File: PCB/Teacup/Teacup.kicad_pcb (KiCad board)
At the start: 2 copper layers, 1 part

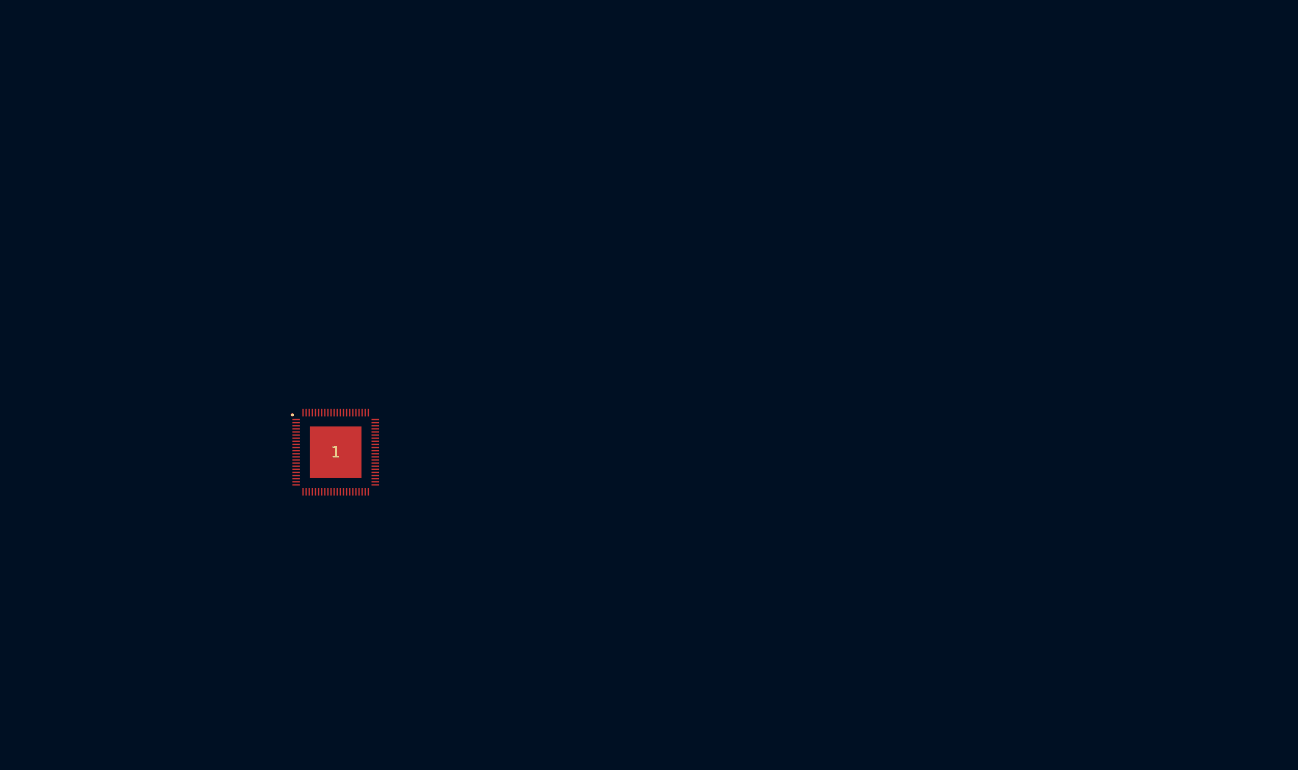
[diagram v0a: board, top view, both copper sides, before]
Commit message: pcb: flash + footprints
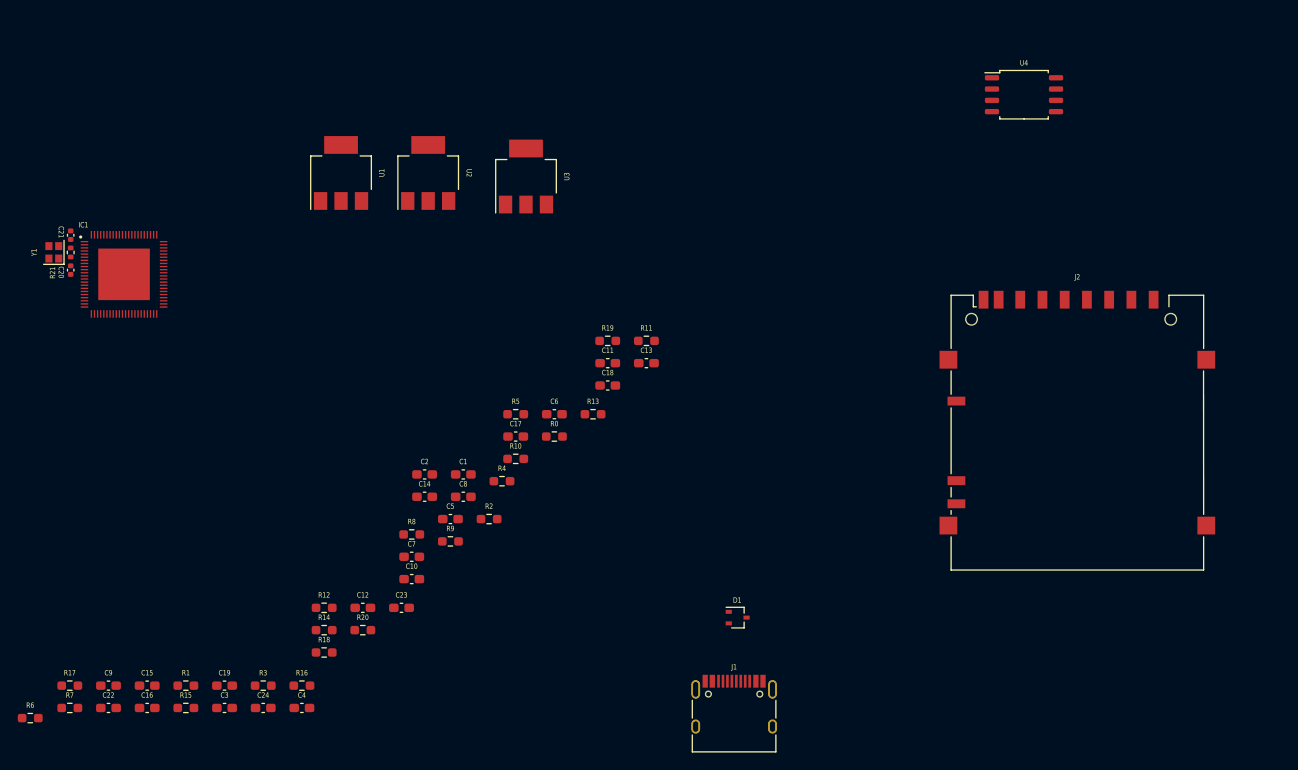
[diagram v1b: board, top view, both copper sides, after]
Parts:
- removed 1: T31ZX, Footprints:QFN35P900X900X90-89N-D
- added C1: 10uF, Capacitor_SMD:C_0603_1608Metric_Pad1.08x0.95mm_HandSolder, F.Cu at (160.2, 101.7)
- added C10: 10uF, Capacitor_SMD:C_0603_1608Metric_Pad1.08x0.95mm_HandSolder, F.Cu at (154.3, 113.5)
- added C11: 1uF, Capacitor_SMD:C_0603_1608Metric_Pad1.08x0.95mm_HandSolder, F.Cu at (176.4, 89.2)
- added C12: 100nF, Capacitor_SMD:C_0603_1608Metric_Pad1.08x0.95mm_HandSolder, F.Cu at (148.8, 116.7)
- added C13: 10uF, Capacitor_SMD:C_0603_1608Metric_Pad1.08x0.95mm_HandSolder, F.Cu at (180.7, 89.2)
- added C14: 1uF, Capacitor_SMD:C_0603_1608Metric_Pad1.08x0.95mm_HandSolder, F.Cu at (155.8, 104.2)
- added C15: 100nF, Capacitor_SMD:C_0603_1608Metric_Pad1.08x0.95mm_HandSolder, F.Cu at (124.6, 125.5)
- added C16: 10uF, Capacitor_SMD:C_0603_1608Metric_Pad1.08x0.95mm_HandSolder, F.Cu at (124.6, 128.0)
- added C17: 1uF, Capacitor_SMD:C_0603_1608Metric_Pad1.08x0.95mm_HandSolder, F.Cu at (166.0, 97.4)
- added C18: 100nF, Capacitor_SMD:C_0603_1608Metric_Pad1.08x0.95mm_HandSolder, F.Cu at (176.4, 91.7)
- added C19: 100nF, Capacitor_SMD:C_0603_1608Metric_Pad1.08x0.95mm_HandSolder, F.Cu at (133.3, 125.5)
- added C2: 1uF, Capacitor_SMD:C_0603_1608Metric_Pad1.08x0.95mm_HandSolder, F.Cu at (155.8, 101.7)
- added C20: TBD, Capacitor_SMD:C_0402_1005Metric, F.Cu at (116.0, 78.7)
- added C21: TBD, Capacitor_SMD:C_0402_1005Metric, F.Cu at (116.0, 74.8)
- added C22: 4.7uF, Capacitor_SMD:C_0603_1608Metric_Pad1.08x0.95mm_HandSolder, F.Cu at (120.2, 128.0)
- added C23: 100nF, Capacitor_SMD:C_0603_1608Metric_Pad1.08x0.95mm_HandSolder, F.Cu at (153.2, 116.7)
- added C24: 100nF, Capacitor_SMD:C_0603_1608Metric_Pad1.08x0.95mm_HandSolder, F.Cu at (137.7, 128.0)
- added C3: 100nF, Capacitor_SMD:C_0603_1608Metric_Pad1.08x0.95mm_HandSolder, F.Cu at (133.3, 128.0)
- added C4: 10uF, Capacitor_SMD:C_0603_1608Metric_Pad1.08x0.95mm_HandSolder, F.Cu at (142.0, 128.0)
- added C5: 1uF, Capacitor_SMD:C_0603_1608Metric_Pad1.08x0.95mm_HandSolder, F.Cu at (158.7, 106.7)
- added C6: 100nF, Capacitor_SMD:C_0603_1608Metric_Pad1.08x0.95mm_HandSolder, F.Cu at (170.4, 94.9)
- added C7: 10uF, Capacitor_SMD:C_0603_1608Metric_Pad1.08x0.95mm_HandSolder, F.Cu at (154.3, 111.0)
- added C8: 1uF, Capacitor_SMD:C_0603_1608Metric_Pad1.08x0.95mm_HandSolder, F.Cu at (160.2, 104.2)
- added C9: 100nF, Capacitor_SMD:C_0603_1608Metric_Pad1.08x0.95mm_HandSolder, F.Cu at (120.2, 125.5)
- added D1: D_TVS_Dual_AAC, Package_TO_SOT_SMD:SOT-323_SC-70, F.Cu at (191.0, 117.8)
- added IC1: T31ZX, Footprints:QFN35P900X900X90-89N-D, F.Cu at (122.0, 79.2)
- added J1: USB_C_Receptacle_USB2.0, Connector_USB:USB_C_Receptacle_HRO_TYPE-C-31-M-12, F.Cu at (190.6, 129.0)
- added J2: SD_Card, Connector_Card:SD_Hirose_DM1AA_SF_PEJ82, F.Cu at (229.2, 97.0)
- added R0: 100k, Resistor_SMD:R_0603_1608Metric_Pad0.98x0.95mm_HandSolder, F.Cu at (170.4, 97.4)
- added R1: 100k, Resistor_SMD:R_0603_1608Metric_Pad0.98x0.95mm_HandSolder, F.Cu at (128.9, 125.5)
- added R10: 100k, Resistor_SMD:R_0603_1608Metric_Pad0.98x0.95mm_HandSolder, F.Cu at (166.0, 100.0)
- added R11: 100k, Resistor_SMD:R_0603_1608Metric_Pad0.98x0.95mm_HandSolder, F.Cu at (180.7, 86.7)
- added R12: 100k, Resistor_SMD:R_0603_1608Metric_Pad0.98x0.95mm_HandSolder, F.Cu at (144.5, 116.7)
- added R13: 100k, Resistor_SMD:R_0603_1608Metric_Pad0.98x0.95mm_HandSolder, F.Cu at (174.7, 94.9)
- added R14: 100k, Resistor_SMD:R_0603_1608Metric_Pad0.98x0.95mm_HandSolder, F.Cu at (144.5, 119.2)
- added R15: 47k, Resistor_SMD:R_0603_1608Metric_Pad0.98x0.95mm_HandSolder, F.Cu at (128.9, 128.0)
- added R16: 47k, Resistor_SMD:R_0603_1608Metric_Pad0.98x0.95mm_HandSolder, F.Cu at (142.0, 125.5)
- added R17: 47k, Resistor_SMD:R_0603_1608Metric_Pad0.98x0.95mm_HandSolder, F.Cu at (115.9, 125.5)
- added R18: 47k, Resistor_SMD:R_0603_1608Metric_Pad0.98x0.95mm_HandSolder, F.Cu at (144.5, 121.7)
- added R19: 47k, Resistor_SMD:R_0603_1608Metric_Pad0.98x0.95mm_HandSolder, F.Cu at (176.4, 86.7)
- added R2: 0R, Resistor_SMD:R_0603_1608Metric_Pad0.98x0.95mm_HandSolder, F.Cu at (163.1, 106.7)
- added R20: 47k, Resistor_SMD:R_0603_1608Metric_Pad0.98x0.95mm_HandSolder, F.Cu at (148.8, 119.2)
- added R21: 1M, Resistor_SMD:R_0402_1005Metric, F.Cu at (116.0, 76.7)
- added R3: 0R, Resistor_SMD:R_0603_1608Metric_Pad0.98x0.95mm_HandSolder, F.Cu at (137.7, 125.5)
- added R4: 5k1, Resistor_SMD:R_0603_1608Metric_Pad0.98x0.95mm_HandSolder, F.Cu at (164.5, 102.5)
- added R5: 5k1, Resistor_SMD:R_0603_1608Metric_Pad0.98x0.95mm_HandSolder, F.Cu at (166.0, 94.9)
- added R6: 0R, Resistor_SMD:R_0603_1608Metric_Pad0.98x0.95mm_HandSolder, F.Cu at (111.5, 129.1)
- added R7: 0R, Resistor_SMD:R_0603_1608Metric_Pad0.98x0.95mm_HandSolder, F.Cu at (115.9, 128.0)
- added R8: 0R, Resistor_SMD:R_0603_1608Metric_Pad0.98x0.95mm_HandSolder, F.Cu at (154.3, 108.5)
- added R9: 0R, Resistor_SMD:R_0603_1608Metric_Pad0.98x0.95mm_HandSolder, F.Cu at (158.7, 109.2)
- added U1: AZ1117-3.3, Kicad:SOT-223-3_TabPin2, F.Cu at (146.4, 67.8)
- added U2: AZ1117-1.8, Kicad:SOT-223-3_TabPin2, F.Cu at (156.2, 67.8)
- added U3: MCP1826S, Kicad:SOT-223-3_TabPin2, F.Cu at (167.2, 68.2)
- added U4: W25Q32JVSS, Package_SO:SOIC-8_5.23x5.23mm_P1.27mm, F.Cu at (223.2, 59.0)
- added Y1: 24 MHz, Crystal:Crystal_SMD_2016-4Pin_2.0x1.6mm, F.Cu at (114.1, 76.7)

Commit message: pcb: sch done, initial placement
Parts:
- added J3: SFW15R-2STE1LF, Footprints:SFW15R2STE1LF, F.Cu at (174.4, 96.3)
- added J4: EXP0, Connector_PinHeader_2.54mm:PinHeader_1x10_P2.54mm_Vertical, F.Cu at (165.4, 85.2)
- added J5: UART, Connector_PinHeader_2.54mm:PinHeader_1x03_P2.54mm_Vertical, F.Cu at (208.9, 54.8)
- added J6: EXP2, Connector_PinHeader_2.54mm:PinHeader_1x16_P2.54mm_Vertical, F.Cu at (165.3, 54.8)
- added J7: EXP1, Connector_PinHeader_2.54mm:PinHeader_1x16_P2.54mm_Vertical, F.Cu at (203.4, 58.4)
- moved R6 136.0 mm to (233.0, 68.0), turned to 90 degrees
- moved C16 134.5 mm to (243.4, 64.8), turned to 180 degrees
- moved C15 131.9 mm to (239.8, 61.2)
- moved R7 128.5 mm to (229.6, 68.0), turned to 90 degrees
- moved C9 128.1 mm to (233.1, 64.8)
- moved C3 111.7 mm to (222.8, 61.2)
- moved R17 110.6 mm to (217.2, 81.0), turned to 90 degrees
- moved R15 103.5 mm to (217.2, 73.8), turned to 90 degrees
- moved R3 99.8 mm to (219.2, 68.0), turned to 90 degrees
- moved C4 99.7 mm to (219.2, 64.8), turned to 180 degrees
- moved C12 98.0 mm to (229.6, 61.2), turned to 180 degrees
- moved R8 94.5 mm to (239.8, 68.0), turned to 90 degrees
- moved R9 94.2 mm to (243.4, 68.0), turned to 90 degrees
- moved C14 93.6 mm to (239.8, 63.0)
- moved C7 93.2 mm to (233.2, 61.2)
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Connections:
- IC1 pad 1: unconnected-(IC1-Pad1) -> Net-(IC1-Pad1)
- IC1 pad 11: unconnected-(IC1-Pad11) -> /CAM_PE
- IC1 pad 12: unconnected-(IC1-Pad12) -> /I2C0_SCK
- IC1 pad 13: unconnected-(IC1-Pad13) -> /I2C0_SDA
- IC1 pad 14: unconnected-(IC1-Pad14) -> /PA17
- IC1 pad 15: unconnected-(IC1-Pad15) -> /PA16
- IC1 pad 16: unconnected-(IC1-Pad16) -> /PA15
- IC1 pad 17: unconnected-(IC1-Pad17) -> /PA14
- IC1 pad 18: unconnected-(IC1-Pad18) -> /PA11
- IC1 pad 19: unconnected-(IC1-Pad19) -> /PA10
- IC1 pad 2: unconnected-(IC1-Pad2) -> Net-(IC1-Pad2)
- IC1 pad 20: unconnected-(IC1-Pad20) -> /PA09
- IC1 pad 21: unconnected-(IC1-Pad21) -> /PA08
- IC1 pad 22: unconnected-(IC1-Pad22) -> /PA07
- IC1 pad 23: unconnected-(IC1-Pad23) -> /PA06
- IC1 pad 24: unconnected-(IC1-Pad24) -> /MIPI_0_N
- IC1 pad 25: unconnected-(IC1-Pad25) -> /MIPI_0_P
- IC1 pad 26: unconnected-(IC1-Pad26) -> /MIPI_CLK_N
- IC1 pad 27: unconnected-(IC1-Pad27) -> /MIPI_CLK_P
- IC1 pad 28: unconnected-(IC1-Pad28) -> /MIPI_1_N
- IC1 pad 29: unconnected-(IC1-Pad29) -> /MIPI_1_P
- IC1 pad 32: unconnected-(IC1-Pad32) -> /AUX0
- IC1 pad 41: unconnected-(IC1-Pad41) -> /MICLP
- IC1 pad 44: unconnected-(IC1-Pad44) -> /HPOUTL
- IC1 pad 57: unconnected-(IC1-Pad57) -> Net-(IC1-Pad57)
- IC1 pad 58: unconnected-(IC1-Pad58) -> Net-(IC1-Pad58)
- IC1 pad 59: unconnected-(IC1-Pad59) -> Net-(IC1-Pad59)
- IC1 pad 60: unconnected-(IC1-Pad60) -> Net-(IC1-Pad60)
- IC1 pad 61: unconnected-(IC1-Pad61) -> Net-(IC1-Pad61)
- IC1 pad 62: unconnected-(IC1-Pad62) -> Net-(IC1-Pad62)
- IC1 pad 63: unconnected-(IC1-Pad63) -> Net-(IC1-Pad63)
- IC1 pad 64: unconnected-(IC1-Pad64) -> Net-(IC1-Pad64)
- IC1 pad 65: unconnected-(IC1-Pad65) -> Net-(IC1-Pad65)
- IC1 pad 66: unconnected-(IC1-Pad66) -> Net-(IC1-Pad66)
- IC1 pad 68: unconnected-(IC1-Pad68) -> Net-(IC1-Pad68)
- IC1 pad 69: unconnected-(IC1-Pad69) -> Net-(IC1-Pad69)
- IC1 pad 70: unconnected-(IC1-Pad70) -> Net-(IC1-Pad70)
- IC1 pad 71: unconnected-(IC1-Pad71) -> Net-(IC1-Pad71)
- IC1 pad 73: unconnected-(IC1-Pad73) -> /UART_RX
- IC1 pad 74: unconnected-(IC1-Pad74) -> /UART_TX
- IC1 pad 80: unconnected-(IC1-Pad80) -> /CAM_LED
- IC1 pad 81: unconnected-(IC1-Pad81) -> /PB30
- IC1 pad 82: unconnected-(IC1-Pad82) -> /PB29
- IC1 pad 85: unconnected-(IC1-Pad85) -> /PB28
- IC1 pad 86: unconnected-(IC1-Pad86) -> /PB27
- IC1 pad 87: unconnected-(IC1-Pad87) -> /PB26
- IC1 pad 88: unconnected-(IC1-Pad88) -> /PB25
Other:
- board outline added: 89.6 x 50.4 mm

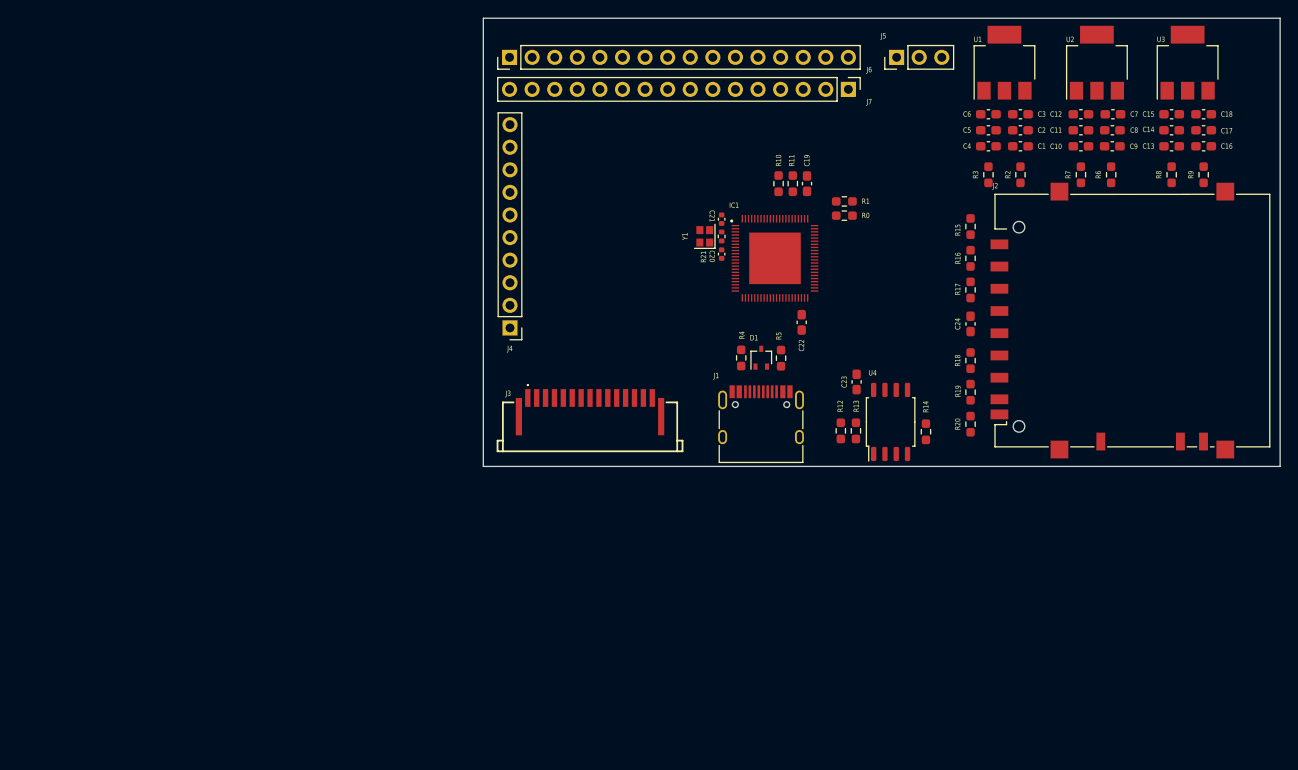
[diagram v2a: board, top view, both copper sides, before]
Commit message: pcb: routed high speed signals
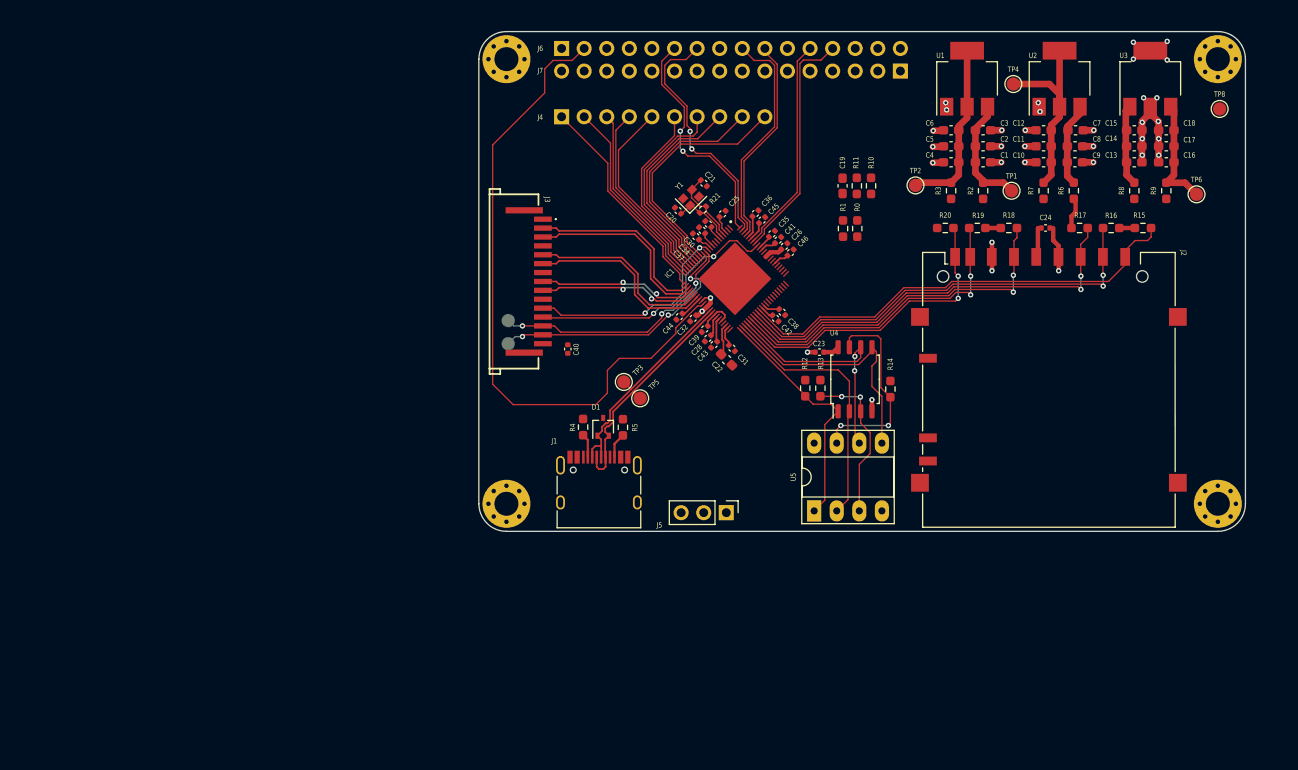
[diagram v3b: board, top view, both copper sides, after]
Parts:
- added C25: 100nF, Capacitor_SMD:C_0402_1005Metric, F.Cu at (189.3, 72.4)
- added C26: 100nF, Capacitor_SMD:C_0402_1005Metric, F.Cu at (196.2, 76.0)
- added C28: 100nF, Capacitor_SMD:C_0402_1005Metric, F.Cu at (187.7, 86.4)
- added C30: 100nF, Capacitor_SMD:C_0402_1005Metric, F.Cu at (187.7, 73.5)
- added C31: 100nF, Capacitor_SMD:C_0402_1005Metric, F.Cu at (190.3, 87.5)
- added C32: 100nF, Capacitor_SMD:C_0402_1005Metric, F.Cu at (186.0, 84.2)
- added C34: 100nF, Capacitor_SMD:C_0402_1005Metric, F.Cu at (187.0, 74.2)
- added C35: 100nF, Capacitor_SMD:C_0402_1005Metric, F.Cu at (194.8, 74.7)
- added C36: 100nF, Capacitor_SMD:C_0402_1005Metric, F.Cu at (193.0, 72.3)
- added C37: 100nF, Capacitor_SMD:C_0402_1005Metric, F.Cu at (186.3, 75.0)
- added C38: 100nF, Capacitor_SMD:C_0402_1005Metric, F.Cu at (196.0, 83.5)
- added C39: 100nF, Capacitor_SMD:C_0402_1005Metric, F.Cu at (187.3, 85.3)
- added C40: 100nF, Capacitor_SMD:C_0402_1005Metric, F.Cu at (171.9, 87.6)
- added C41: 100nF, Capacitor_SMD:C_0402_1005Metric, F.Cu at (195.6, 75.3)
- added C42: 100nF, Capacitor_SMD:C_0402_1005Metric, F.Cu at (195.2, 84.2)
- added C43: 100nF, Capacitor_SMD:C_0402_1005Metric, F.Cu at (188.3, 87.1)
- added C44: 100nF, Capacitor_SMD:C_0402_1005Metric, F.Cu at (184.4, 84.0)
- added C45: 100nF, Capacitor_SMD:C_0402_1005Metric, F.Cu at (193.8, 73.1)
- added C46: 100nF, Capacitor_SMD:C_0402_1005Metric, F.Cu at (196.9, 76.8)
- added REF**: MountingHole_2.7mm_M2.5_Pad_Via, MountingHole:MountingHole_2.7mm_M2.5_Pad_Via, F.Cu at (245.0, 55.0)
- added REF**: MountingHole_2.7mm_M2.5_Pad_Via, MountingHole:MountingHole_2.7mm_M2.5_Pad_Via, F.Cu at (245.0, 105.0)
- added REF**: MountingHole_2.7mm_M2.5_Pad_Via, MountingHole:MountingHole_2.7mm_M2.5_Pad_Via, F.Cu at (165.0, 105.0)
- added REF**: MountingHole_2.7mm_M2.5_Pad_Via, MountingHole:MountingHole_2.7mm_M2.5_Pad_Via, F.Cu at (165.0, 55.0)
- added TP1: TestPoint, TestPoint:TestPoint_Pad_D1.5mm, F.Cu at (221.8, 69.8)
- added TP2: TestPoint, TestPoint:TestPoint_Pad_D1.5mm, F.Cu at (211.0, 69.2)
- added TP3: TestPoint, TestPoint:TestPoint_Pad_D1.5mm, F.Cu at (178.2, 91.3)
- added TP4: TestPoint, TestPoint:TestPoint_Pad_D1.5mm, F.Cu at (222.0, 57.8)
- added TP5: TestPoint, TestPoint:TestPoint_Pad_D1.5mm, F.Cu at (180.0, 93.1)
- added TP6: TestPoint, TestPoint:TestPoint_Pad_D1.5mm, F.Cu at (242.6, 70.2)
- added TP7: TestPoint, TestPoint:TestPoint_Pad_D1.5mm, B.Cu at (165.2, 87.0)
- added TP8: TestPoint, TestPoint:TestPoint_Pad_D1.5mm, F.Cu at (245.2, 60.6)
- added TP9: TestPoint, TestPoint:TestPoint_Pad_D1.5mm, B.Cu at (165.2, 84.4)
- added U5: W25Q32JVSS, Package_DIP:DIP-8_W7.62mm_Socket_LongPads, F.Cu at (199.6, 105.8)
- C23, C24: footprint Capacitor_SMD:C_0603_1608Metric_Pad1.08x0.95mm_HandSolder -> Capacitor_SMD:C_0402_1005Metric
- J1: value USB_C_Receptacle_USB2.0 -> USB Type-C
- moved J5 54.7 mm to (189.7, 106.0), turned to -90 degrees
- moved J4 24.4 mm to (171.2, 61.5), turned to 90 degrees
- moved R20 22.2 mm to (214.3, 74.0), turned to 0 degrees
- moved J1 19.7 mm to (175.4, 103.8)
- moved R4 19.4 mm to (173.6, 96.4)
- moved R5 19.4 mm to (178.1, 96.4)
- moved D1 19.4 mm to (175.9, 96.3)
- moved R15 19.4 mm to (236.6, 74.0), turned to 0 degrees
- moved R19 18.5 mm to (217.9, 74.0), turned to 180 degrees
- moved J3 18.5 mm to (165.8, 80.0), turned to -90 degrees
- moved R16 16.2 mm to (233.0, 74.0), turned to 180 degrees
- moved R18 15.5 mm to (221.5, 74.0), turned to 0 degrees
- moved R17 14.1 mm to (229.4, 74.0), turned to 0 degrees
- moved C24 13.7 mm to (225.6, 74.0), turned to 0 degrees
- moved J2 12.2 mm to (226.0, 92.2), turned to 0 degrees
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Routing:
- net /AUX0: track 0.00 -> 74.5 mm
- net /MMC0_D2: track 0.00 -> 51.6 mm
- net /MMC0_D3: track 0.00 -> 49.1 mm, vias 0 -> 2
- net /MMC0_CMD: track 0.00 -> 47.6 mm, vias 0 -> 2
- net /MMC0_CLK: track 0.00 -> 40.4 mm, vias 0 -> 2
- net GND: track 0.00 -> 37.5 mm, vias 0 -> 33
- net /MMC0_D0: track 0.00 -> 36.0 mm, vias 0 -> 2
- net /MMC0_D1: track 0.00 -> 35.2 mm, vias 0 -> 2
- net /I2C0_SDA: track 0.00 -> 29.8 mm, vias 0 -> 3
- net /CAM_LED: track 0.00 -> 29.8 mm, vias 0 -> 2
- net /NOR_DR: track 0.00 -> 29.7 mm
- net /NOR_DT: track 0.00 -> 28.9 mm
- net /I2C0_SCK: track 0.00 -> 28.8 mm, vias 0 -> 3
- net /PB26: track 0.00 -> 27.7 mm, vias 0 -> 2
- net /NOR_CK: track 0.00 -> 27.3 mm, vias 0 -> 2
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- added copper zone on In1.Cu, net GND
- added copper zone on In2.Cu, net GND
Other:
- board size 89.6 x 50.4 mm -> 86.2 x 56.2 mm
- copper layers 2 -> 4
